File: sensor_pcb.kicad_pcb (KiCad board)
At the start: 2 copper layers, 50 x 80 mm, 35 parts, among them J1 RTDSensor, J3 Conn_01x08, U1 MAX31865, U2 MIC5225, U3 74LVC125

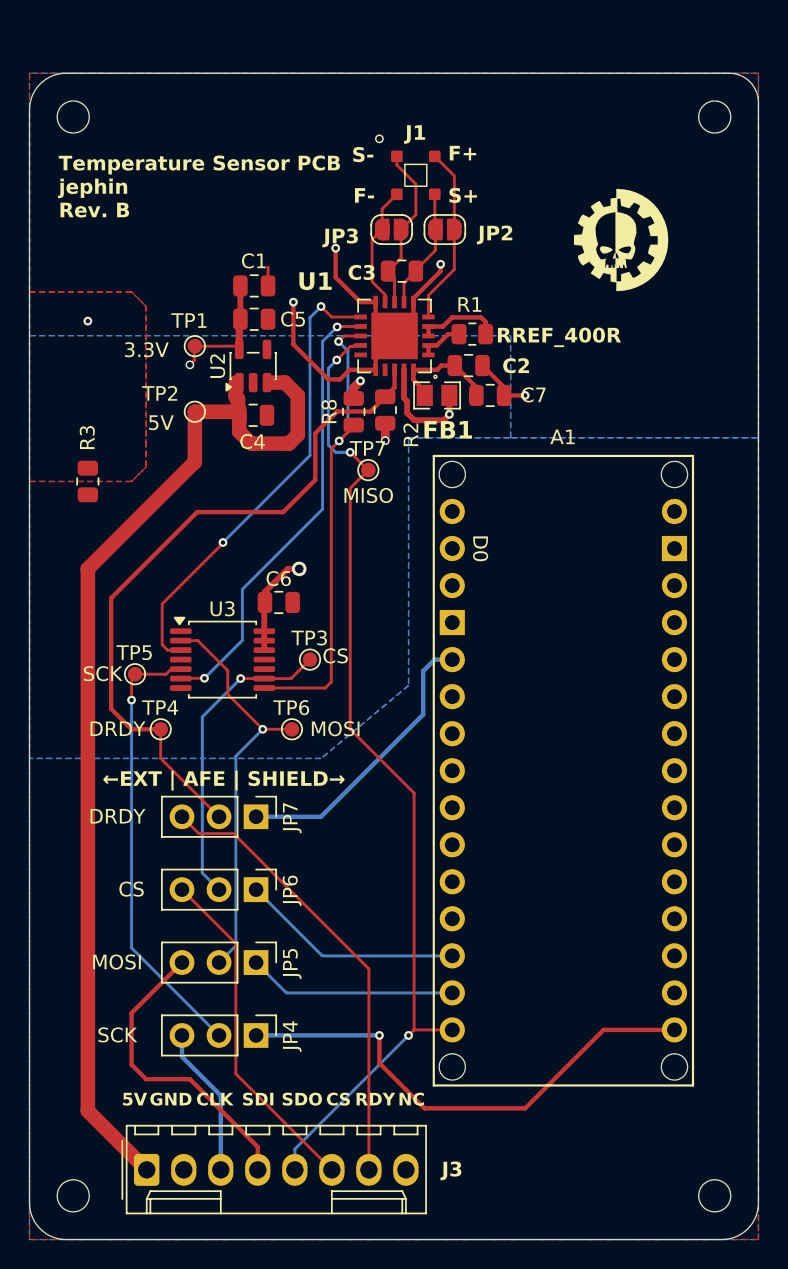
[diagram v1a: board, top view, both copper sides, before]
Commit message: RTD sensor wire bonding landing pattern interdigitated
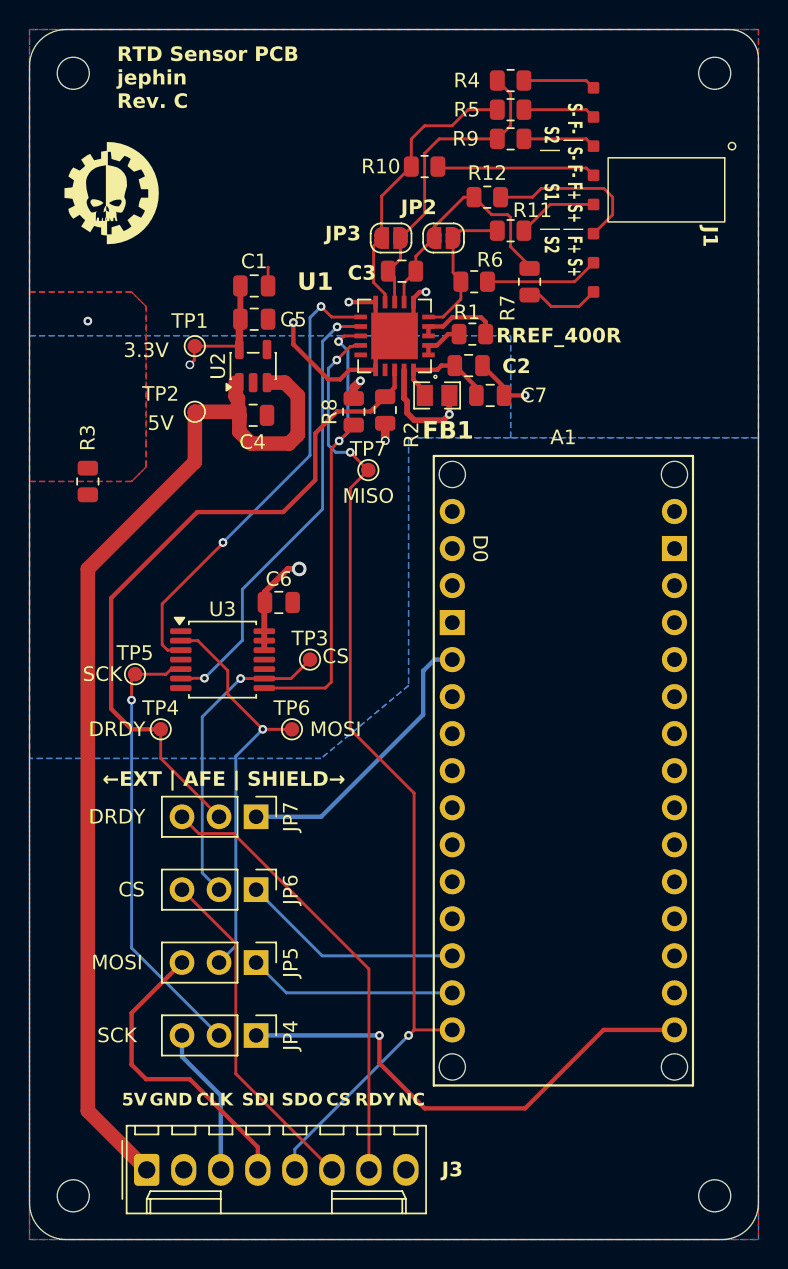
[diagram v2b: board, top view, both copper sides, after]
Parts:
- added R10: 0, Resistor_SMD:R_0805_2012Metric, F.Cu at (127.1, 76.4)
- added R11: 0, Resistor_SMD:R_0805_2012Metric, F.Cu at (133.0, 80.8)
- added R12: 0, Resistor_SMD:R_0805_2012Metric, F.Cu at (131.4, 78.5)
- added R4: 0, Resistor_SMD:R_0805_2012Metric, F.Cu at (133.0, 70.5)
- added R5: 0, Resistor_SMD:R_0805_2012Metric, F.Cu at (133.0, 72.5)
- added R6: 0, Resistor_SMD:R_0805_2012Metric, F.Cu at (130.5, 84.3)
- added R7: 0, Resistor_SMD:R_0805_2012Metric, F.Cu at (134.3, 84.3)
- added R9: 0, Resistor_SMD:R_0805_2012Metric, F.Cu at (133.0, 74.5)
- J1: footprint external_footprints:RTD_Sensor_BondPad_4x -> external_footprints:RTD_Sensor_BondPad_interdigitated
- moved J1 13.2 mm to (139.7, 78.0), turned to -90 degrees
- moved U$18 3.00 mm to (103.0, 70.0)
- moved U$19 3.00 mm to (147.0, 70.0)
- moved JP2 0.59 mm to (128.4, 81.3)
- moved JP3 0.58 mm to (124.8, 81.3)
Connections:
- C3 pad 1: /SENSOR_S+ -> /AFE_S+
- C3 pad 2: /SENSOR_S- -> /AFE_S-
- J1 pad 1: /SENSOR_S- -> /S1_S-
- J1 pad 2: /SENSOR_F+ -> /S1_F-
- J1 pad 3: /SENSOR_F- -> /S1_F+
- J1 pad 4: /SENSOR_S+ -> /S1_S+
- JP2 pad 1: /SENSOR_S+ -> /AFE_S+
- JP2 pad 2: /SENSOR_F+ -> /AFE_F+
- JP3 pad 1: /SENSOR_F- -> /AFE_F-
- JP3 pad 2: /SENSOR_S- -> /AFE_S-
- U1 pad 5: /SENSOR_F+ -> /AFE_F+
- U1 pad 7: /SENSOR_S+ -> /AFE_S+
- U1 pad 8: /SENSOR_S- -> /AFE_S-
- U1 pad 9: /SENSOR_F- -> /AFE_F-
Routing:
- net /AFE_S-: track 0.00 -> 21.6 mm
- net /AFE_F-: track 0.00 -> 19.3 mm
- net /AFE_S+: track 0.00 -> 16.8 mm
- net /SENSOR_F+: track 12.3 -> 0.00 mm
- net /SENSOR_S-: track 11.5 -> 0.00 mm
- net /S1_S+: track 0.00 -> 11.2 mm
- net /S1_F-: track 0.00 -> 10.8 mm
- net /AFE_F+: track 0.00 -> 10.3 mm
- net /SENSOR_F-: track 8.47 -> 0.00 mm
- net /S2_F+: track 0.00 -> 7.81 mm
- net /SENSOR_S+: track 7.61 -> 0.00 mm
- net GNDA: track 25.0 -> 17.9 mm
- net /S1_F+: track 0.00 -> 5.52 mm
- net /S2_S-: track 0.00 -> 4.98 mm
- net /S2_F-: track 0.00 -> 4.98 mm
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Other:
- board size 50 x 80 mm -> 50 x 83 mm
- board text added: "RTD Sensor PCB jephin Rev. C"
- board text removed: "Temperature Sensor PCB jephin Rev. B"

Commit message: Updated GND/GNDA planes
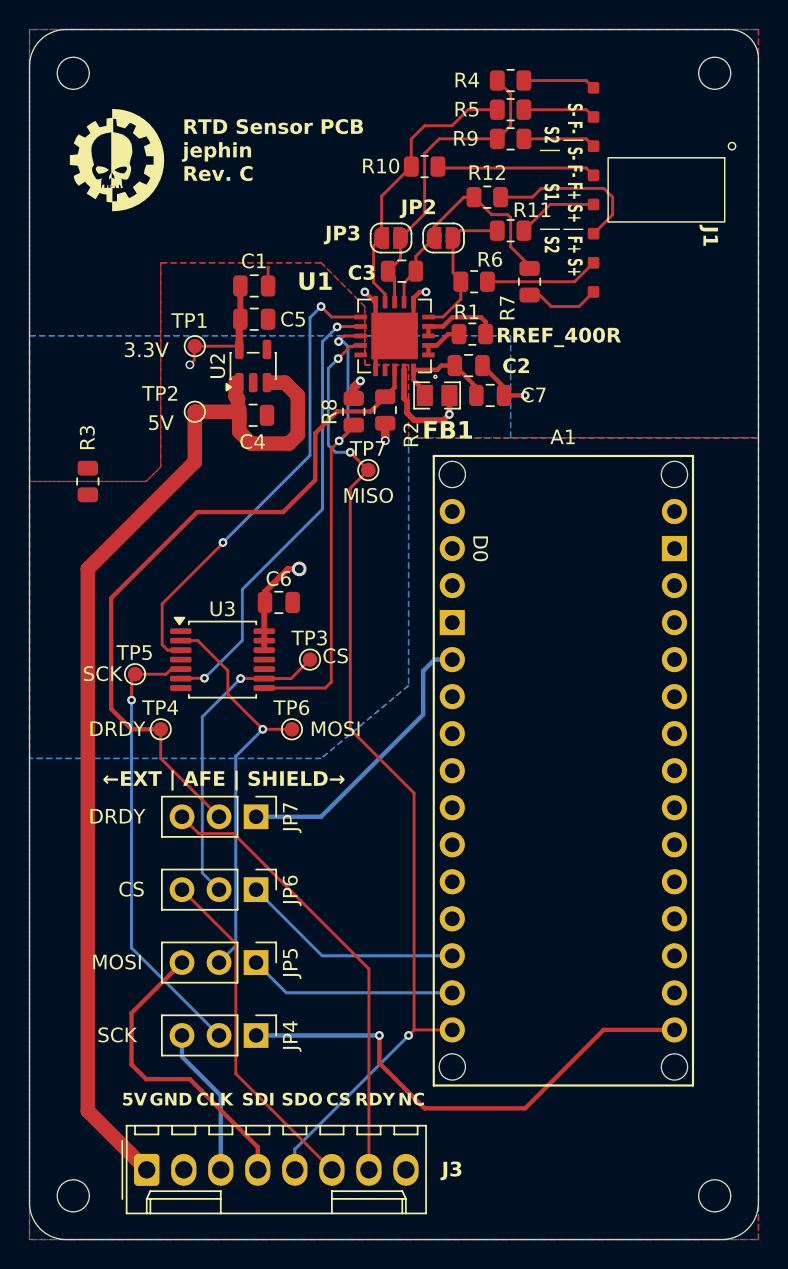
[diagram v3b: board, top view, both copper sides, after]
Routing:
- net GNDA: track 17.9 -> 8.68 mm, vias 5 -> 3

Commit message: Revision C of layout
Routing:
- net GNDA: track 8.68 -> 6.66 mm, vias 3 -> 2
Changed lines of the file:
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@@
-	)
-	(segment
-		(start 122.24 91.56)
-		(end 122.7 91.1)
-		(width 0.6)
-		(layer "F.Cu")
-		(net 33)
 	)
 	(segment
@@
 	)
 	(segment
+		(start 122.6 91.2)
+		(end 122.24 91.56)
+		(width 0.6)
+		(layer "F.Cu")
+		(net 33)
+	)
+	(segment
 		(start 124.4 94.0125)
 		(end 124.4 95.2)
@@
 	)
 	(segment
-		(start 122.24 92.3075)
-		(end 122.24 91.56)
-		(width 0.6)
-		(layer "F.Cu")
-		(net 33)
-	)
-	(segment
 		(start 126.4 93.8)
 		(end 125.9 93.3)
@@
 	)
 	(segment
+		(start 122.24 91.56)
+		(end 122.24 92.3075)
+		(width 0.6)
+		(layer "F.Cu")
+		(net 33)
+	)
+	(segment
 		(start 128.8 93.4)
 		(end 128.8 92.1)
@@
 	)
 	(via
-		(at 122.7 91.1)
+		(at 122.6 91.2)
 		(size 0.6)
 		(drill 0.3)
@@
 	)
 	(segment
-		(start 126.77 85)
-		(end 126.34 85.43)
-		(width 0.3)
-		(layer "F.Cu")
-		(net 49)
-	)
-	(segment
 		(start 123.74 89.32)
 		(end 123.74 90.345)
@@
 	)
 	(segment
-		(start 123 85)
-		(end 123.695 85.695)
-		(width 0.3)
-		(layer "F.Cu")
-		(net 49)
-	)
-	(segment
 		(start 134 92.1)
 		(end 132.55 92.1)
-		(width 0.3)
-		(layer "F.Cu")
-		(net 49)
-	)
-	(segment
-		(start 127.2 85)
-		(end 126.77 85)
 		(width 0.3)
 		(layer "F.Cu")
@@
 	)
 	(via
-		(at 127.2 85)
+		(at 128 85)
 		(size 0.6)
 		(drill 0.3)
 		(layers "F.Cu" "B.Cu")
-		(net 49)
-	)
-	(via
-		(at 123 85)
-		(size 0.6)
-		(drill 0.3)
-		(layers "F.Cu" "B.Cu")
-		(free yes)
 		(net 49)
 	)
@@
 		(net_name "GNDA")
 		(layer "F.Cu")
-		(name "GNDD")
+		(name "GNDA")
 		(hatch edge 0.5)
 		(priority 3)
